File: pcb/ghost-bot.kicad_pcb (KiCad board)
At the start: 2 copper layers, 31 parts, among them J1 Conn_01x03_Pin, J2 Conn_01x03_Pin, J3 Conn_01x02_Pin, J4 Conn_01x04_Pin, J5 Conn_01x05_Pin, J6 Conn_01x05_Pin, J7 Conn_01x05_Pin, J8 Conn_01x05_Pin, SW1 SW_Push, SW2 SW_Push

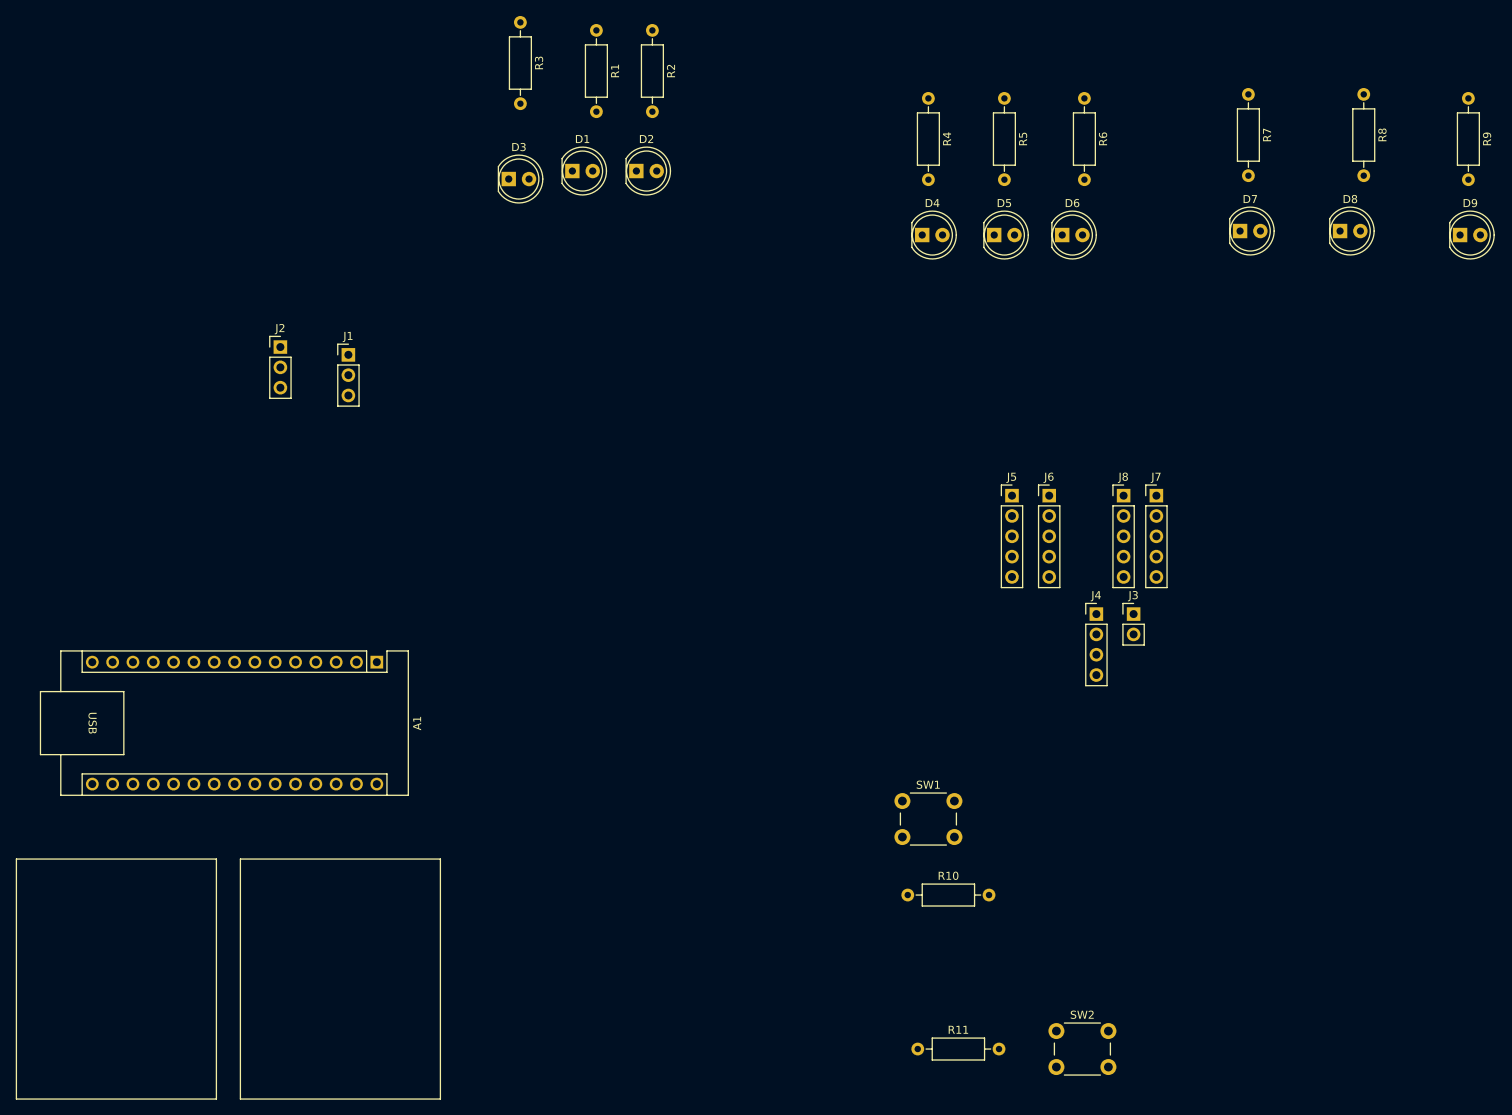
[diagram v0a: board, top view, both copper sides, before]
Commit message: Add ghost outline edgecut, place components
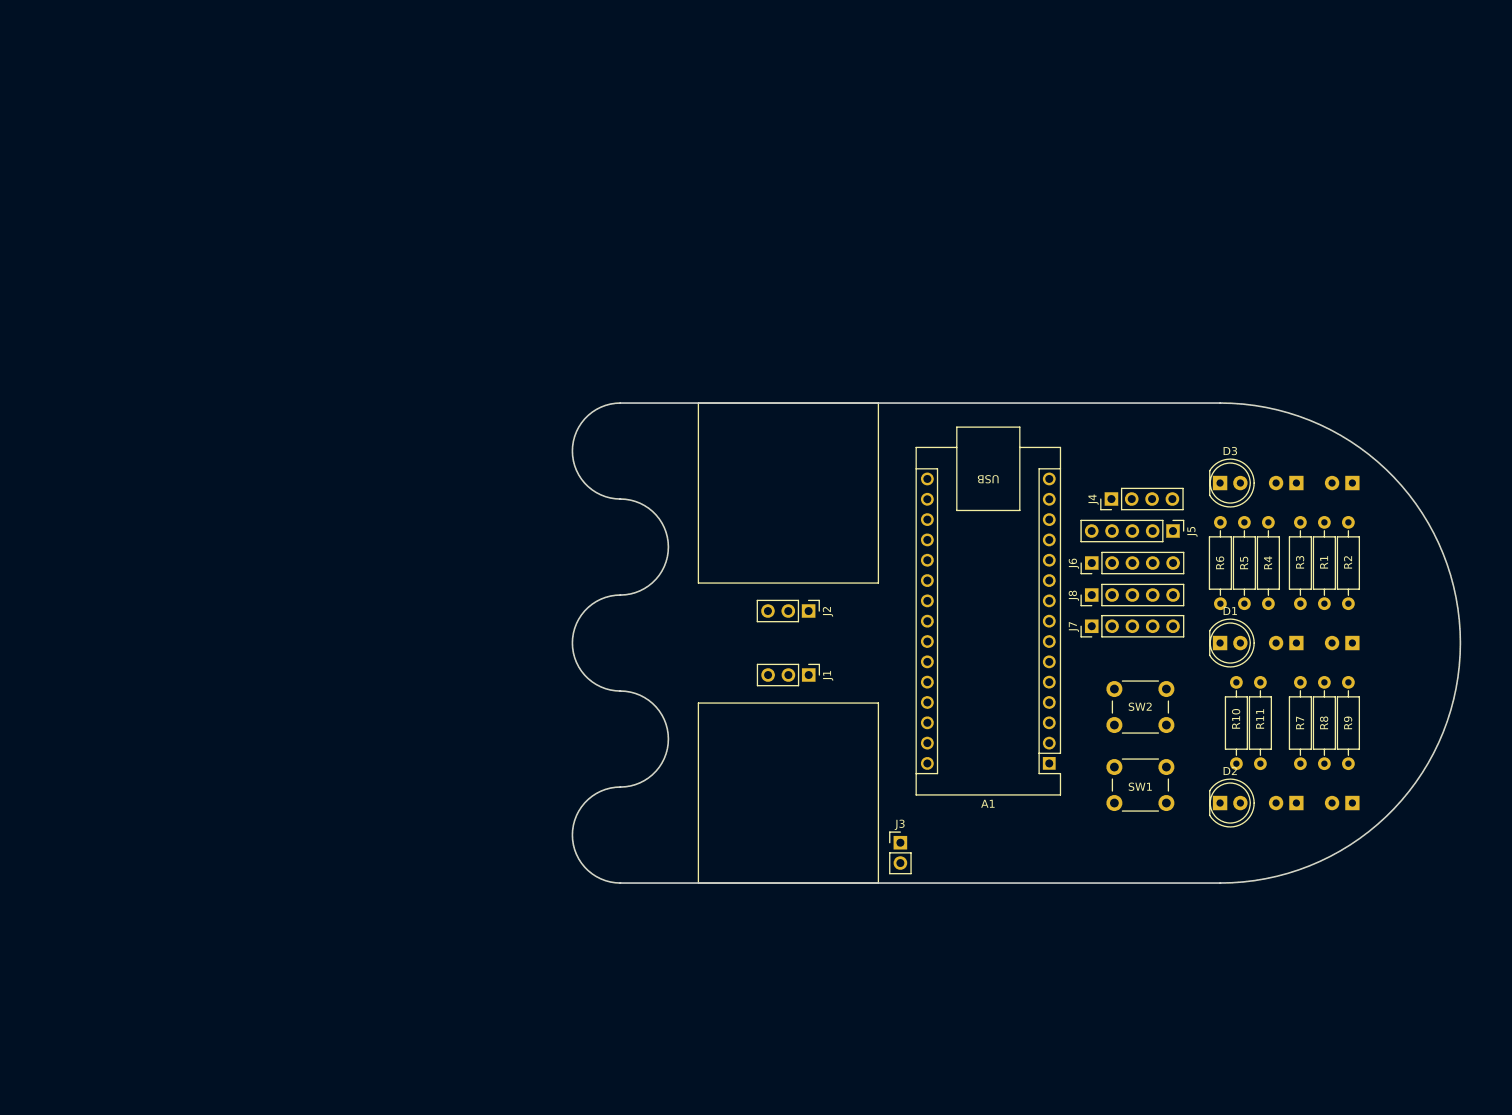
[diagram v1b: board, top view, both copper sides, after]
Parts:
- D4, D5, D6, D7, D8, D9: moved to B.Cu
- moved R3 121.6 mm to (192.5, 109.1), turned to 90 degrees
- moved R1 115.8 mm to (195.5, 109.1), turned to 90 degrees
- moved R2 112.7 mm to (198.5, 109.1), turned to 90 degrees
- moved D2 107.5 mm to (182.5, 134.0)
- moved D1 100.2 mm to (182.5, 114.0)
- moved D3 96.7 mm to (182.5, 94.0)
- moved D4 89.1 mm to (199.0, 134.0), turned to 180 degrees
- moved A1 85.0 mm to (161.1, 129.1), turned to 180 degrees
- moved R9 84.5 mm to (198.5, 129.1), turned to 90 degrees
- moved R7 83.9 mm to (192.5, 129.1), turned to 90 degrees
- moved R8 83.8 mm to (195.5, 129.1), turned to 90 degrees
- moved R4 76.1 mm to (188.5, 109.1), turned to 90 degrees
- moved D9 73.9 mm to (192.0, 134.0), turned to 180 degrees
- moved J2 73.8 mm to (131.0, 110.0), turned to -90 degrees
- moved J1 70.1 mm to (131.0, 118.0), turned to -90 degrees
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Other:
- board outline added: 111 x 60 mm

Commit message: Random commit before refactoring
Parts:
- moved J4 37.1 mm to (164.5, 132.8), turned to 180 degrees
- moved J3 16.0 mm to (158.5, 138.0)
- moved J5 13.0 mm to (175.6, 87.0)
- moved J6 13.0 mm to (165.4, 91.0)
- moved J7 13.0 mm to (165.4, 98.9)
- moved J8 13.0 mm to (165.4, 95.0)
- moved J1 7.42 mm to (127.5, 111.5), turned to 0 degrees
- moved A1 3.61 mm to (158.1, 127.0)
- moved J2 1.55 mm to (131.5, 111.5), turned to 0 degrees

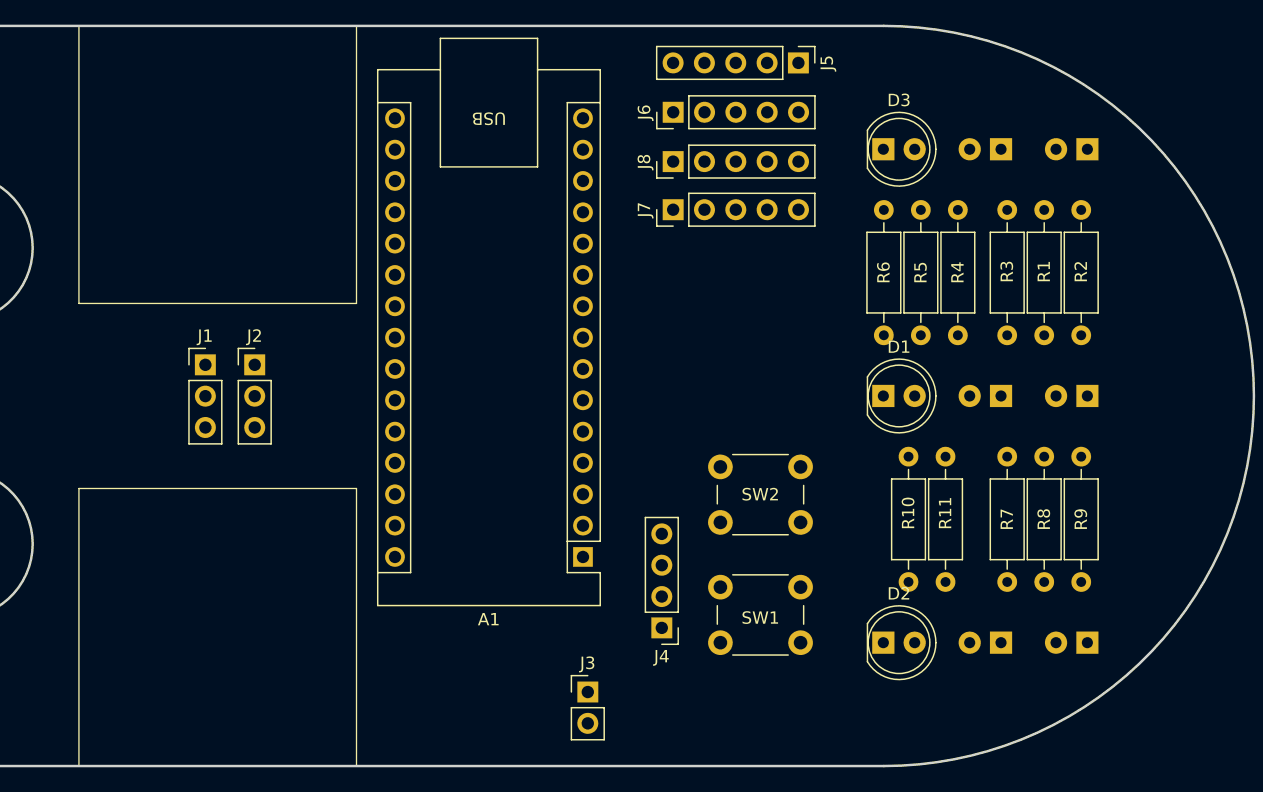
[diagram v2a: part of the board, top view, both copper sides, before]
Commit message: Simplify circuit, add battery holder mounting points
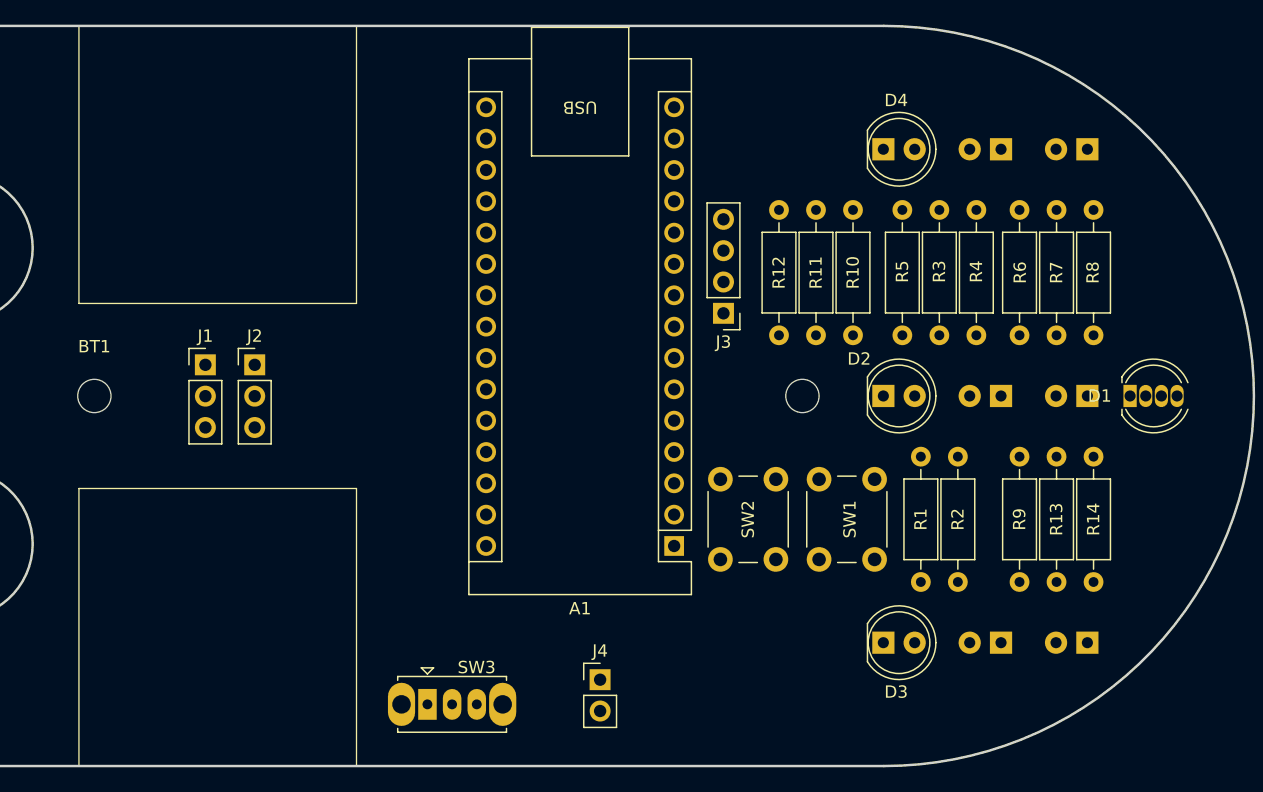
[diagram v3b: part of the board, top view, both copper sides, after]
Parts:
- removed J5, J6, J7, J8: Conn_01x05_Pin, Connector_PinHeader_2.54mm:PinHeader_1x05_P2.54mm_Vertical
- added BT1: Battery Holder, ghost-bot-footprints:Keystone 2478 Battery Holder, F.Cu at (118.5, 114.0)
- added D1: LED_BKGR, LED_THT:LED_D5.0mm-4_RGB, F.Cu at (202.5, 114.0)
- added R6: 150R, Resistor_THT:R_Axial_DIN0207_L6.3mm_D2.5mm_P10.16mm_Horizontal, F.Cu at (193.5, 109.1)
- added R7: 85R, Resistor_THT:R_Axial_DIN0207_L6.3mm_D2.5mm_P10.16mm_Horizontal, F.Cu at (196.5, 109.1)
- added R8: 85R, Resistor_THT:R_Axial_DIN0207_L6.3mm_D2.5mm_P10.16mm_Horizontal, F.Cu at (199.5, 109.1)
- added SW3: SW_SPDT, Button_Switch_THT:SW_Slide_SPDT_Straight_CK_OS102011MS2Q, F.Cu at (145.5, 139.0)
- D10: renamed from D9; footprint LED_THT:LED_D5.0mm -> LED_THT:LED_D5.0mm_Clear
- D5: renamed from D7; footprint LED_THT:LED_D5.0mm -> LED_THT:LED_D5.0mm_Clear
- D6: renamed from D4; footprint LED_THT:LED_D5.0mm -> LED_THT:LED_D5.0mm_IRBlack
- D7: renamed from D5; footprint LED_THT:LED_D5.0mm -> LED_THT:LED_D5.0mm_IRBlack
- D8: renamed from D6; footprint LED_THT:LED_D5.0mm -> LED_THT:LED_D5.0mm_IRBlack
- D9: renamed from D8; footprint LED_THT:LED_D5.0mm -> LED_THT:LED_D5.0mm_Clear
- moved J3 26.0 mm to (169.5, 107.3)
- moved SW1 14.5 mm to (181.8, 120.8), turned to -90 degrees
- moved R10 8.50 mm to (180.0, 109.1)
- moved R11 8.50 mm to (177.0, 109.1)
- moved R12 8.50 mm to (174.0, 109.1)
- moved R3 8.50 mm to (187.0, 109.1)
- moved R4 8.50 mm to (190.0, 109.1)
- moved R5 8.50 mm to (184.0, 109.1)
- moved SW2 7.50 mm to (169.2, 127.2), turned to 90 degrees
- moved A1 7.44 mm to (165.5, 126.2)
- moved J4 1.41 mm to (159.5, 137.0)
- moved R1 1.00 mm to (185.5, 129.1)
- moved R13 1.00 mm to (196.5, 129.1)
- moved R14 1.00 mm to (199.5, 129.1)
- moved R2 1.00 mm to (188.5, 129.1)
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- renumbered D1 to D2, D2 to D3, D3 to D4, J4 to J3, J3 to J4, R10 to R1, R4 to R10, R5 to R11, R6 to R12, R8 to R13, R9 to R14, R11 to R2, R1 to R3, R2 to R4, R3 to R5, R7 to R9
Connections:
- A1 pad 10: /D7 -> unconnected-(A1-D7-Pad10)
- A1 pad 11: /D8 -> unconnected-(A1-D8-Pad11)
- A1 pad 12: /D9 -> /RGB_R
- A1 pad 13: /D10 -> /RGB_G
- A1 pad 14: /D11 -> /RGB_B
- A1 pad 22: /A3 -> unconnected-(A1-A3-Pad22)
- A1 pad 23: /A4 -> unconnected-(A1-A4-Pad23)
- A1 pad 24: /A5 -> unconnected-(A1-A5-Pad24)
- A1 pad 25: /A6 -> unconnected-(A1-A6-Pad25)
- A1 pad 26: /A7 -> unconnected-(A1-A7-Pad26)
- A1 pad 30: +BATT -> +BATT_SW

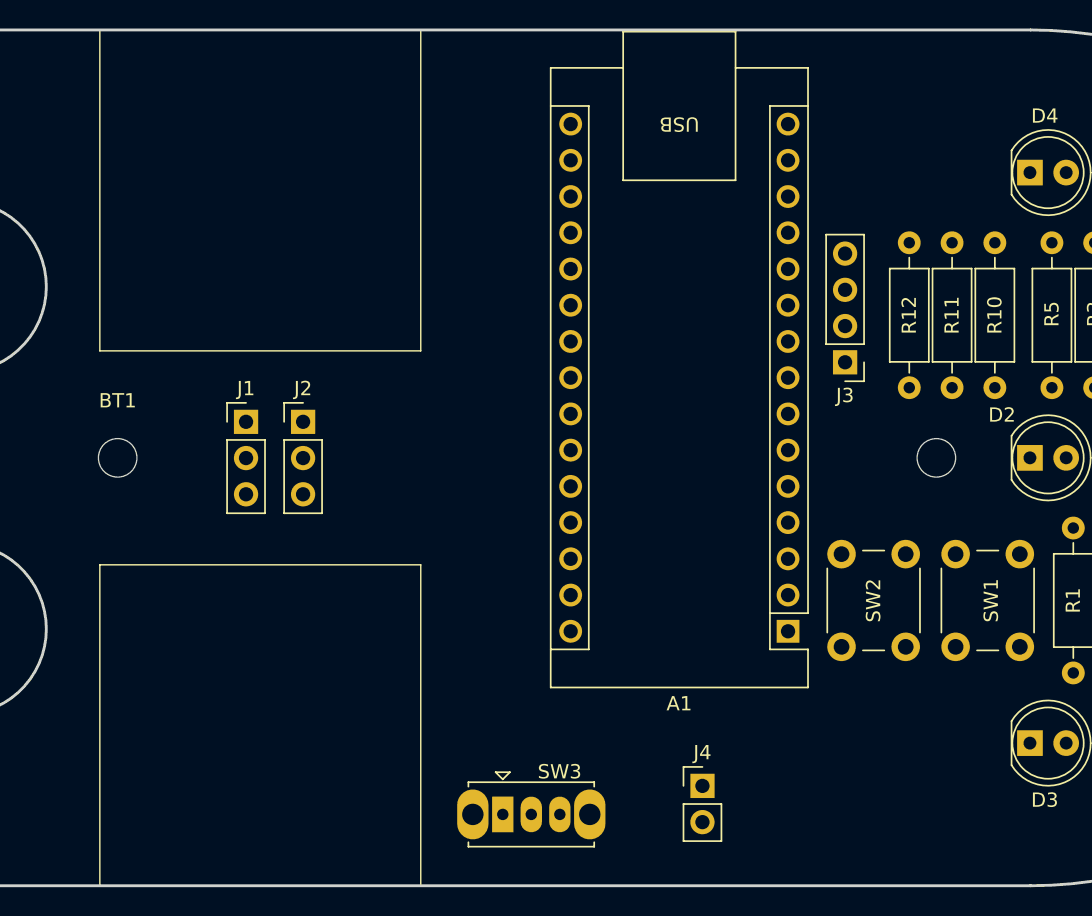
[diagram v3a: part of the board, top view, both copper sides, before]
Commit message: Add footprints for servos
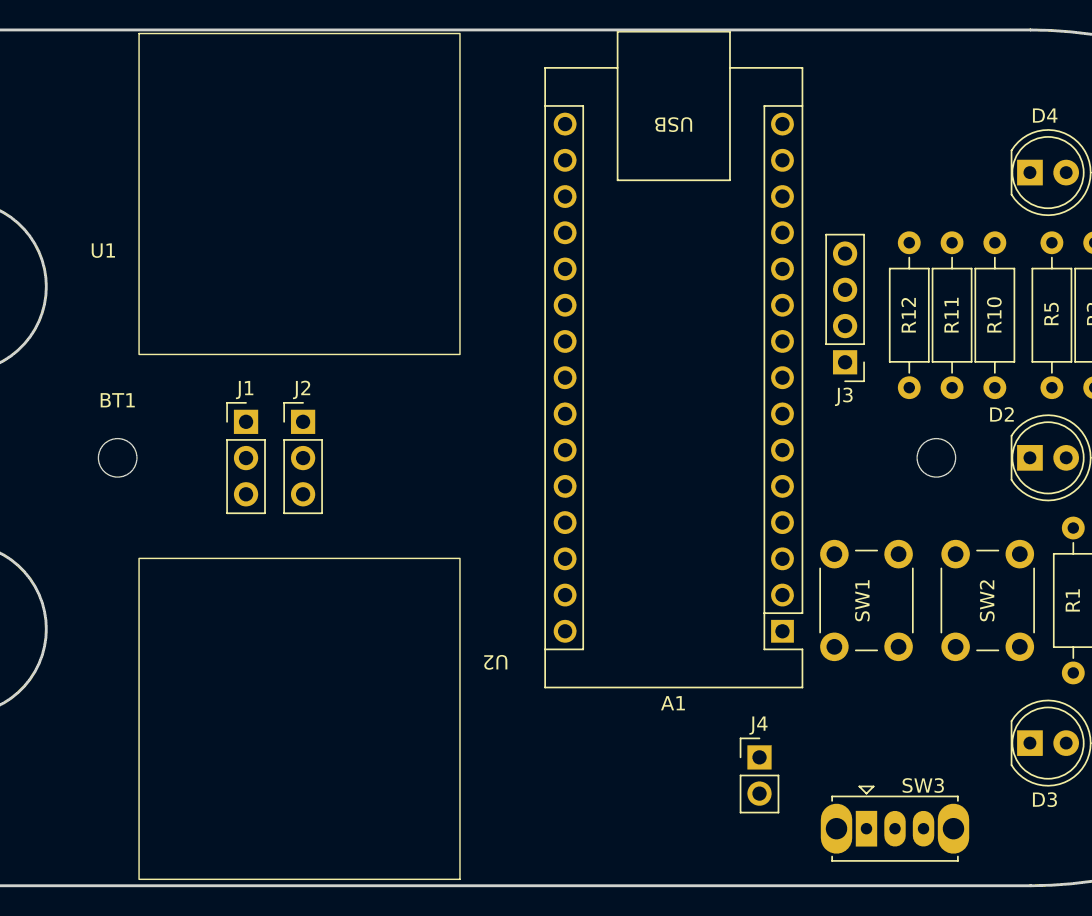
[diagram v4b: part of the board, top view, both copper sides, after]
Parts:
- added U1: ~, ghost-bot-footprints:SG90 Mount, F.Cu at (120.0, 84.2)
- added U2: ~, ghost-bot-footprints:SG90 Mount, F.Cu at (142.5, 143.6)
- moved SW3 25.5 mm to (171.0, 140.0)
- moved SW1 14.5 mm to (168.8, 127.2), turned to 90 degrees
- moved SW2 14.1 mm to (181.8, 120.8), turned to -90 degrees
- moved J4 4.47 mm to (163.5, 135.0)
- moved A1 0.39 mm to (165.1, 126.2)
